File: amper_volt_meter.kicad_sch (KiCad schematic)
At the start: 0 parts

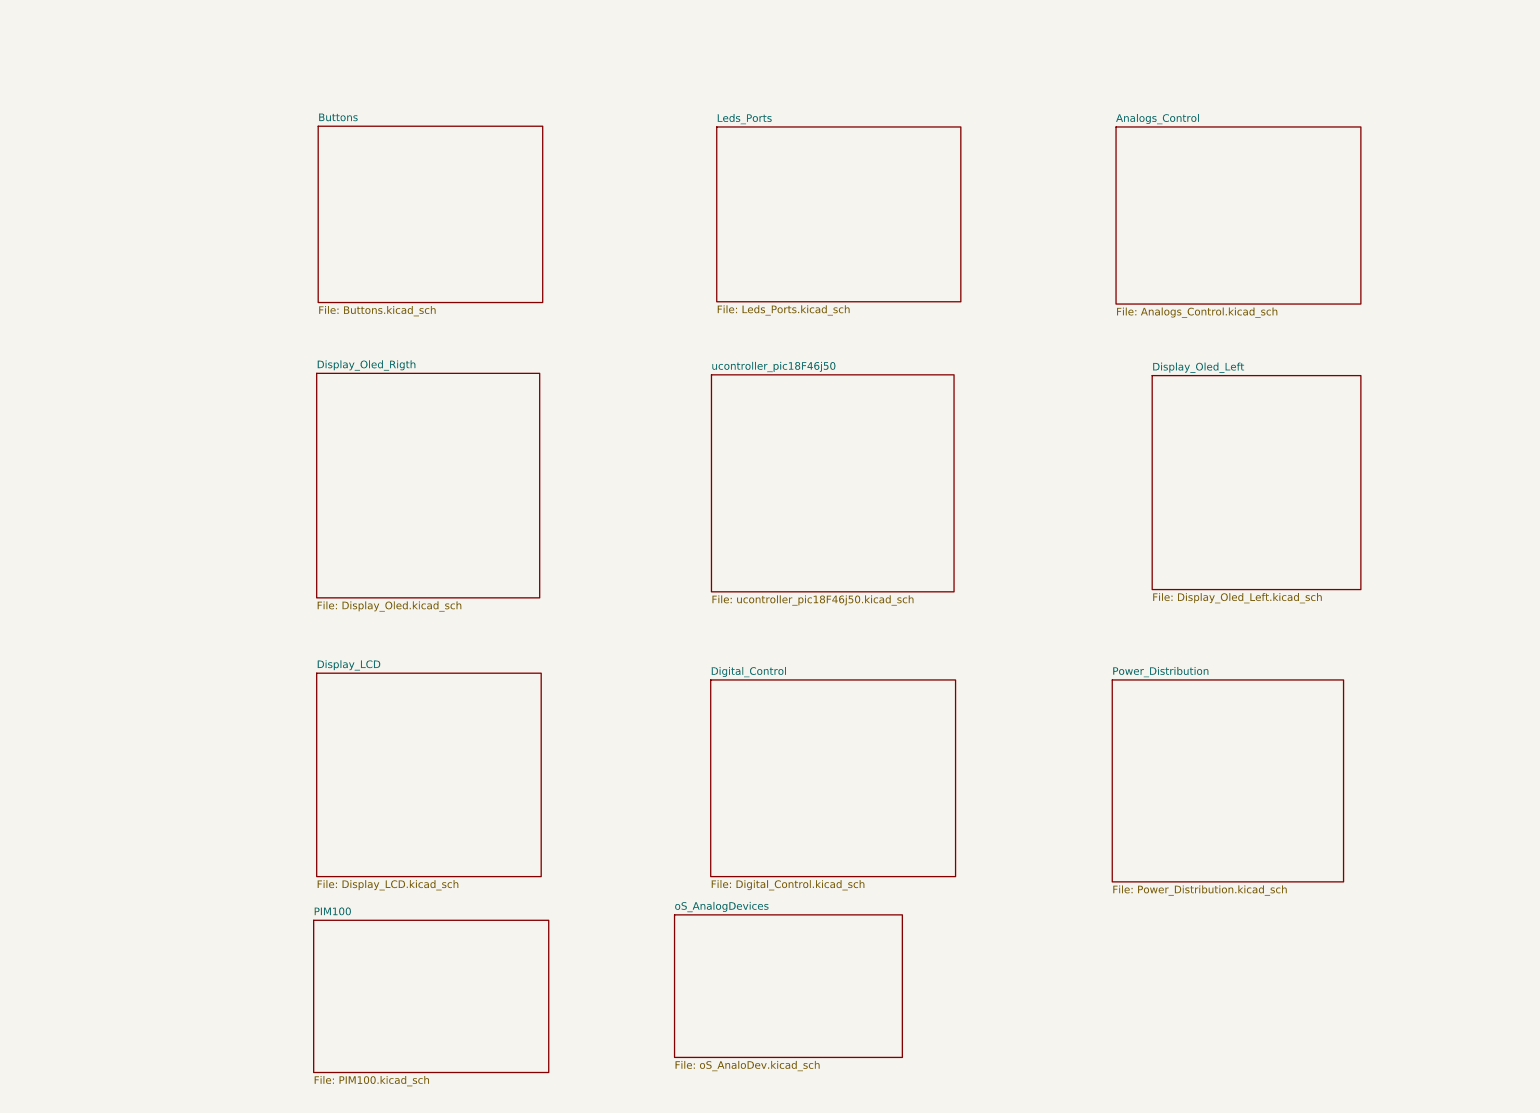
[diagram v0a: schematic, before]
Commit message: feat: agregar hierarchical_labels con nombres correctos a oS_AnaloDev (DiscoveryAnalog3) - 30 pines
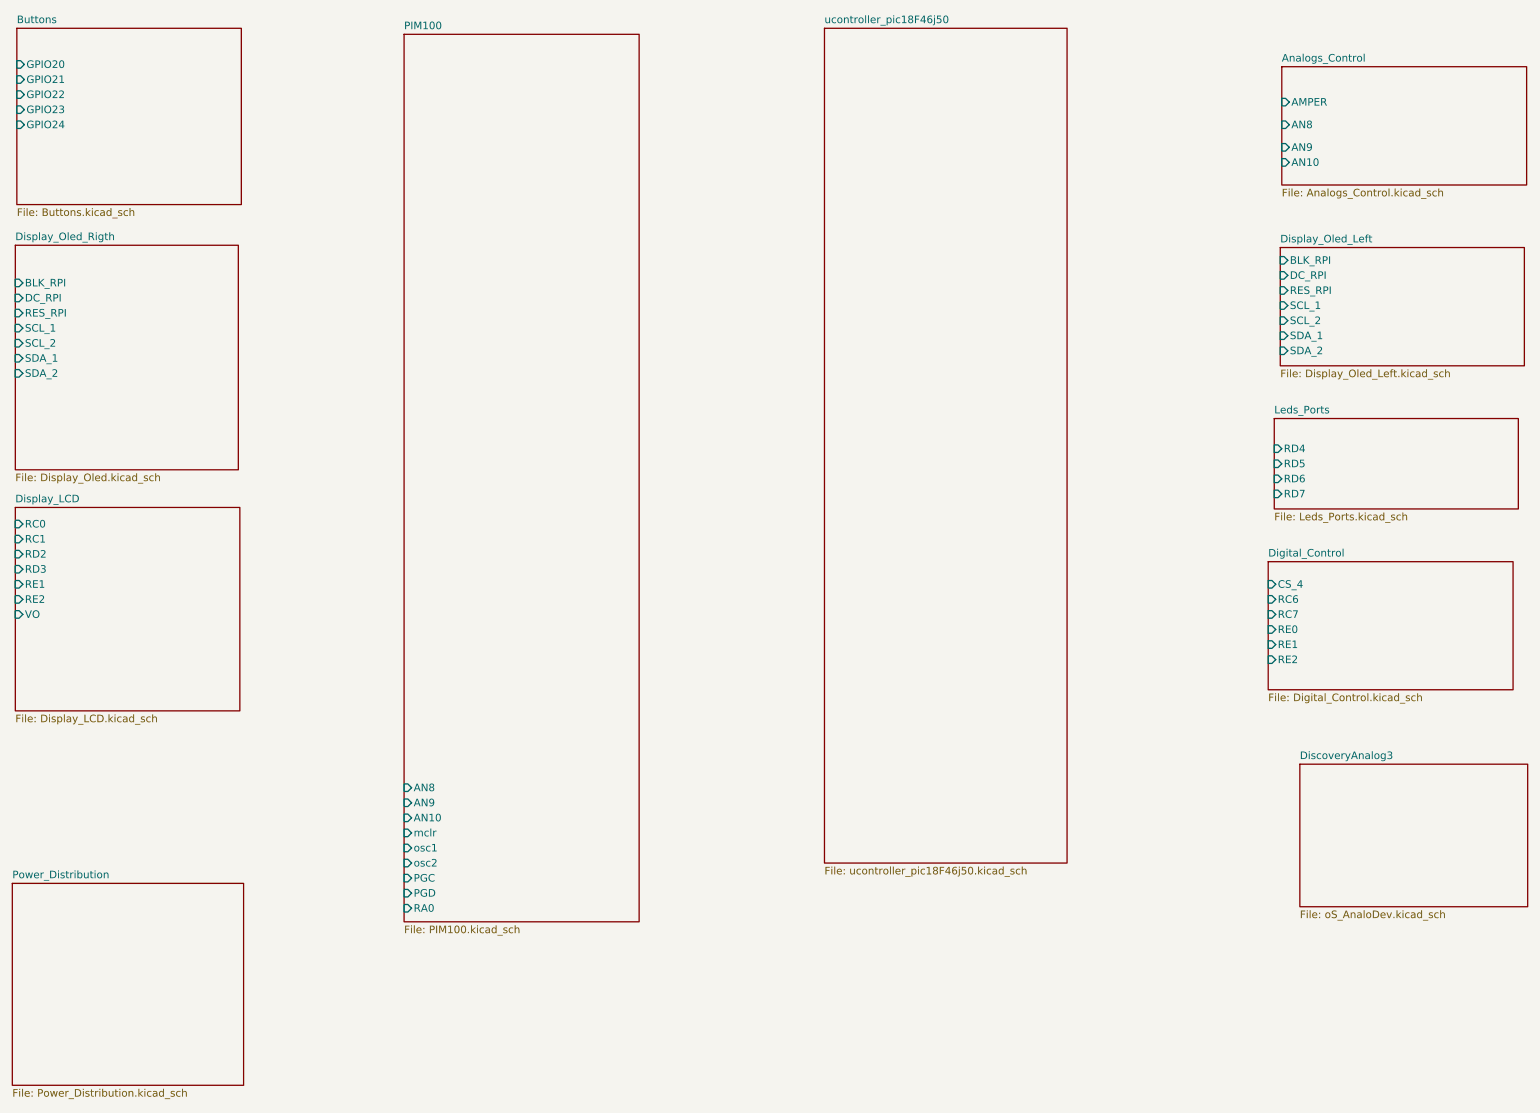
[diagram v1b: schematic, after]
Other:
- sheet oS_AnalogDevices renamed DiscoveryAnalog3
- sheet Analogs_Control ports: added AMPER, AN10, AN8, AN9; removed none
- sheet Buttons ports: added GPIO20, GPIO21, GPIO22, GPIO23, GPIO24; removed none
- sheet Digital_Control ports: added CS_4, RC6, RC7, RE0, RE1, RE2; removed none
- sheet Display_LCD ports: added RC0, RC1, RD2, RD3, RE1, RE2, VO; removed none
- sheet Display_Oled_Left ports: added BLK_RPI, DC_RPI, RES_RPI, SCL_1, SCL_2, SDA_1, SDA_2; removed none
- sheet Display_Oled_Rigth ports: added BLK_RPI, DC_RPI, RES_RPI, SCL_1, SCL_2, SDA_1, SDA_2; removed none
- sheet Leds_Ports ports: added RD4, RD5, RD6, RD7; removed none
- sheet PIM100 ports: added AN10, AN8, AN9, PGC, PGD, RA0, mclr, osc1, osc2; removed none

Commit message: feat: PIM100 - labels en mayusculas y pines externos ordenados por puerto (85 pines, 42 izq + 43 der)
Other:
- sheet PIM100 ports: added MCLR, OSC1, OSC2, RA1, RA10, RA14, RA15, RA4, RA5, RA6, RA7, RA9, RB0, RB10, RB11, RB12, RB13, RB14, RB15, RB6, RB7, RB8, RB9, RC1, RC13, RC14, RC2, RC3, RC4, RD0, RD1, RD10, RD11, RD12, RD13, RD14, RD15, RD2, RD3, RD4, RD5, RD6, RD7, RD8, RD9, RE0, RE1, RE2, RE3, RE4, RE5, RE6, RE7, RE8, RE9, RF0, RF1, RF12, RF13, RF2, RF3, RF4, RF5, RF8, RG0, RG1, RG12, RG13, RG14, RG15, RG6, RG7, RG8, RG9, VBUS, VREF+, VREF-, rg2_d+, rg3_d-; removed mclr, osc1, osc2
